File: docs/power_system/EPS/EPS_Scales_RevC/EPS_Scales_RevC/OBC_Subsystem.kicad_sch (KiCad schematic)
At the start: 5 parts, among them U8 INA230

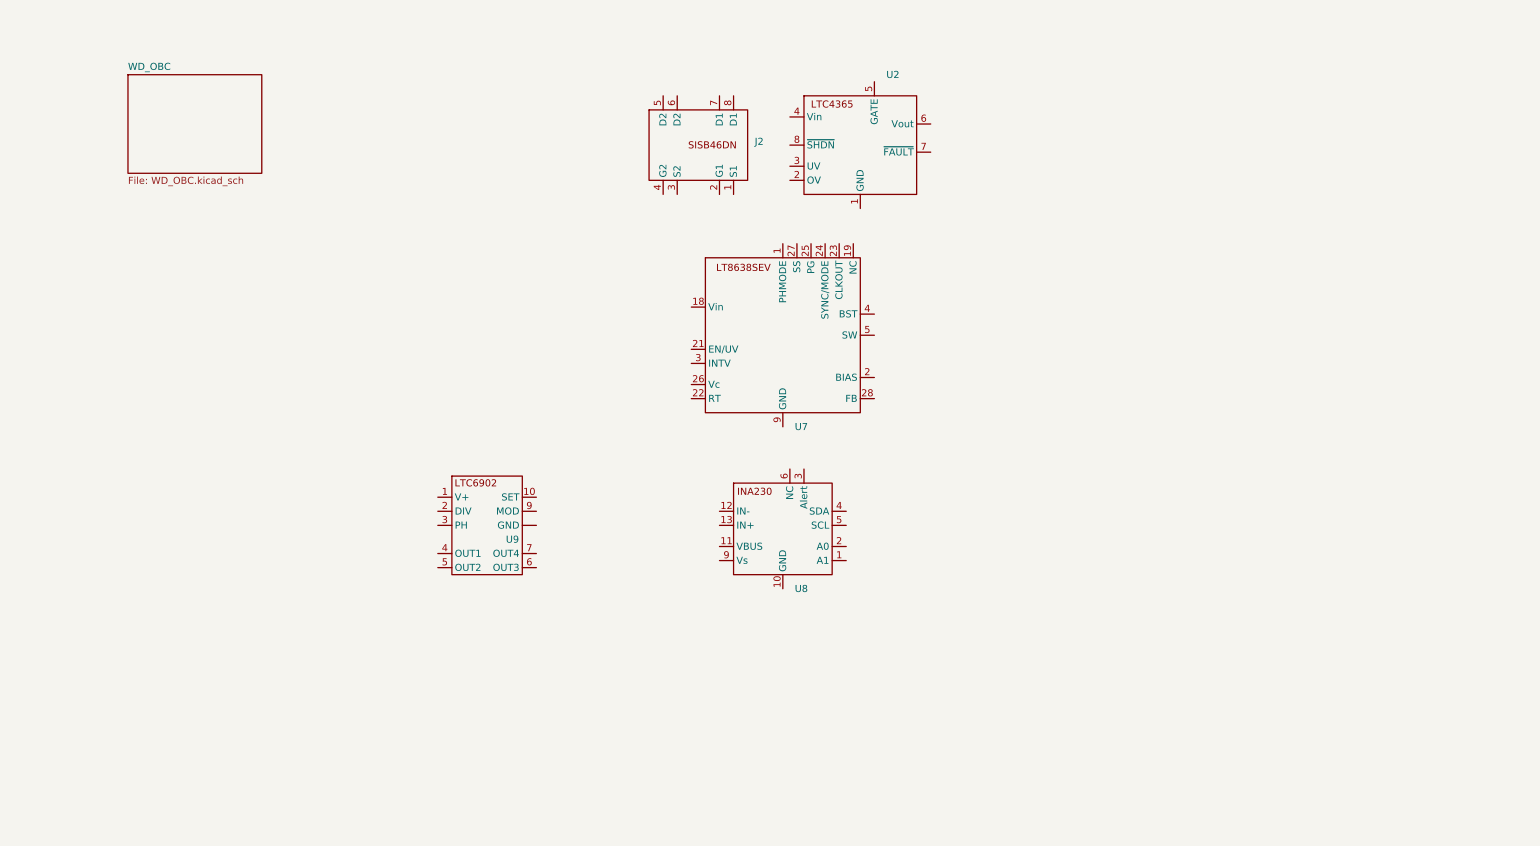
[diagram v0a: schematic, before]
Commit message: Calculations
Lots of behind the scenes stuff going on. Ran through calculations for the Load Switch, Switching Regulator and clock for the jetson using the information from each datasheet. Having to modify these parameters for each subsystem is time consuming as each one requires new calculations. Once this bit is done the schematic will be done, leading to layout. Aiming for thursday Layout.
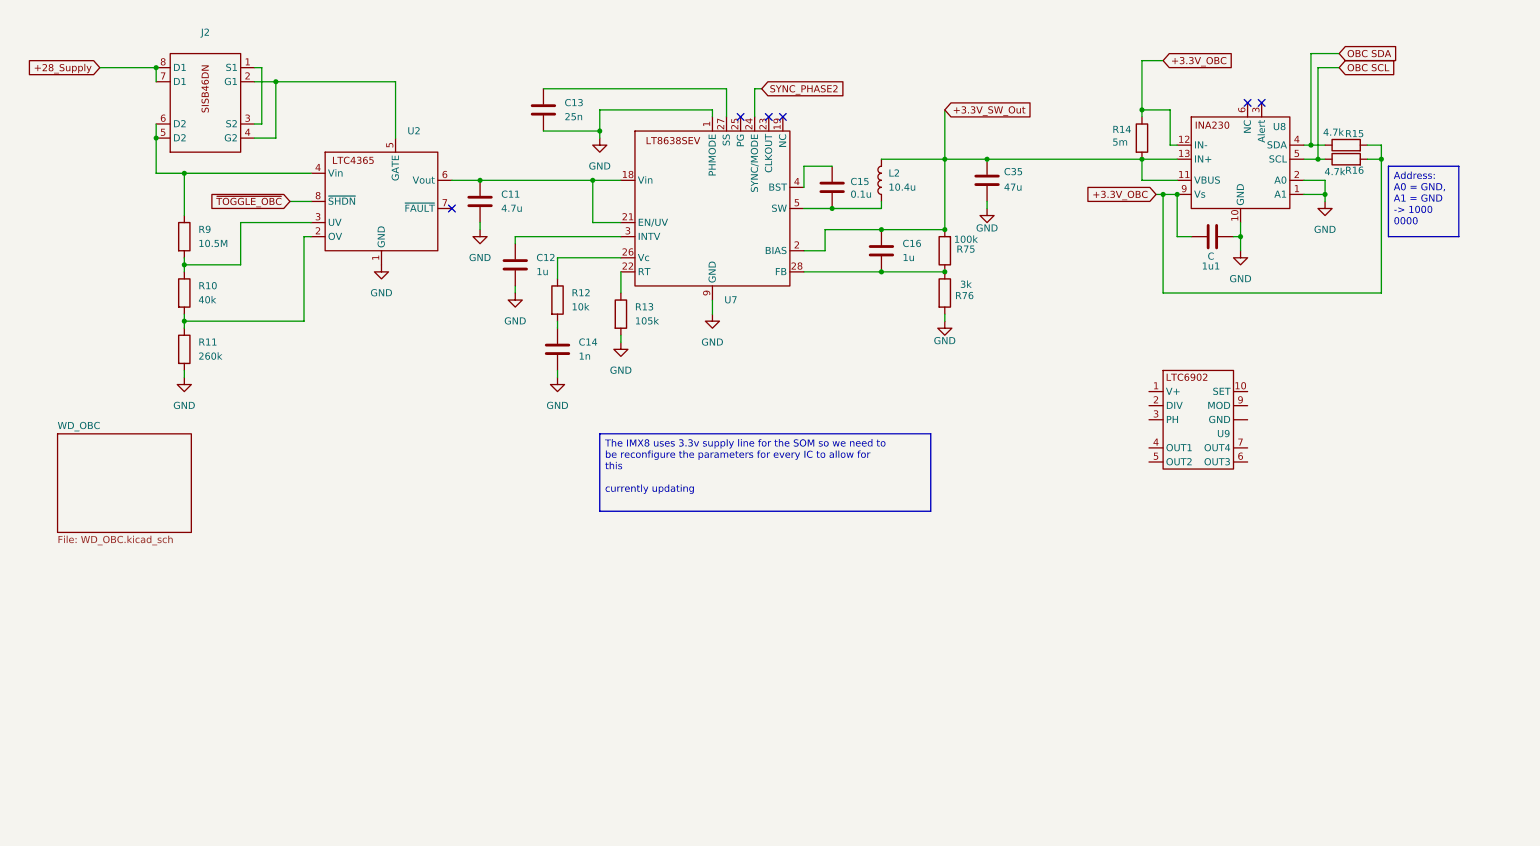
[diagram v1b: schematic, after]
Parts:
- added 1u1: C, symbol Device:C
- added C11: 4.7u, symbol Device:C
- added C12, C16: 1u, symbol Device:C
- added C13: 25n, symbol Device:C
- added C14: 1n, symbol Device:C
- added C15: 0.1u, symbol Device:C
- added C35: 47u, symbol Device:C
- added L2: 10.4u, symbol Device:L
- added R10: 40k, symbol Device:R
- added R11: 260k, symbol Device:R
- added R12: 10k, symbol Device:R
- added R13: 105k, symbol Device:R
- added R14: 5m, symbol Device:R
- added R15, R16: 4.7k, symbol Device:R
- added R75: 100k, symbol Device:R
- added R76: 3k, symbol Device:R
- added R9: 10.5M, symbol Device:R
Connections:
- net GND: now reaches U8.1 (A1)
- net GND: now also U2.1 (GND), U7.1 (PHMODE), U7.9 (GND), U8.10 (GND), U8.2 (A0), 1u1.1, C11.2, C12.2, C13.2, C14.2, C35.2, R11.2, R13.2, R76.2
- net +3.3V_SW_Out: now reaches U8.11 (VBUS)
- net +3.3V_SW_Out: now also U7.2 (BIAS), U8.13 (IN+), C16.1, C35.1, L2.2, R14.2, R75.2
- net +3.3V_OBC: now reaches U8.12 (IN-)
- net +3.3V_OBC: now also U8.9 (Vs), 1u1.2, R14.1, R15.2, R16.2
- net OBC SDA: now reaches U8.4 (SDA)
- net OBC SDA: now also R15.1
- net OBC SCL: now reaches U8.5 (SCL)
- net OBC SCL: now also R16.1
- net at U7.18 (Vin): now also U2.6 (Vout), U7.21 (EN/UV), C11.1
- net at U7.22 (RT): now also R13.1
- net SYNC_PHASE2: now reaches U7.24 (SYNC/MODE)
- net at U7.26 (Vc): now also R12.1
- net at U7.27 (SS): now also C13.1
- net at U7.28 (FB): now also C16.2, R75.1, R76.1
- net at U7.3 (INTV): now also C12.1
- net at U7.4 (BST): now also C15.1
- net at U7.5 (SW): now also C15.2, L2.1
- net at J2.1 (S1): now also J2.3 (S2)
- net at J2.2 (G1): now also J2.4 (G2), U2.5 (GATE)
- net at J2.5 (D2): now also J2.6 (D2), U2.4 (Vin), R9.1
- net +28_Supply: now reaches J2.7 (D1)
- net +28_Supply: now also J2.8 (D1)
- net at U2.2 (OV): now also R10.2, R11.1
- net at U2.3 (UV): now also R10.1, R9.2
- net ~{TOGGLE_OBC}: now reaches U2.8 (~{SHDN})
- new net: C14.1, R12.2
- no-connect marks 0 -> 6
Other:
- moved on the sheet: U9

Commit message: Rev C. Schematic 90 % Complete
All EPS components for each subsystem implemented. Only errors and warning are relating to missing peripheral connections and connectors which will be discussed tomorrow when I go to the lab.
Calculations are done as well.
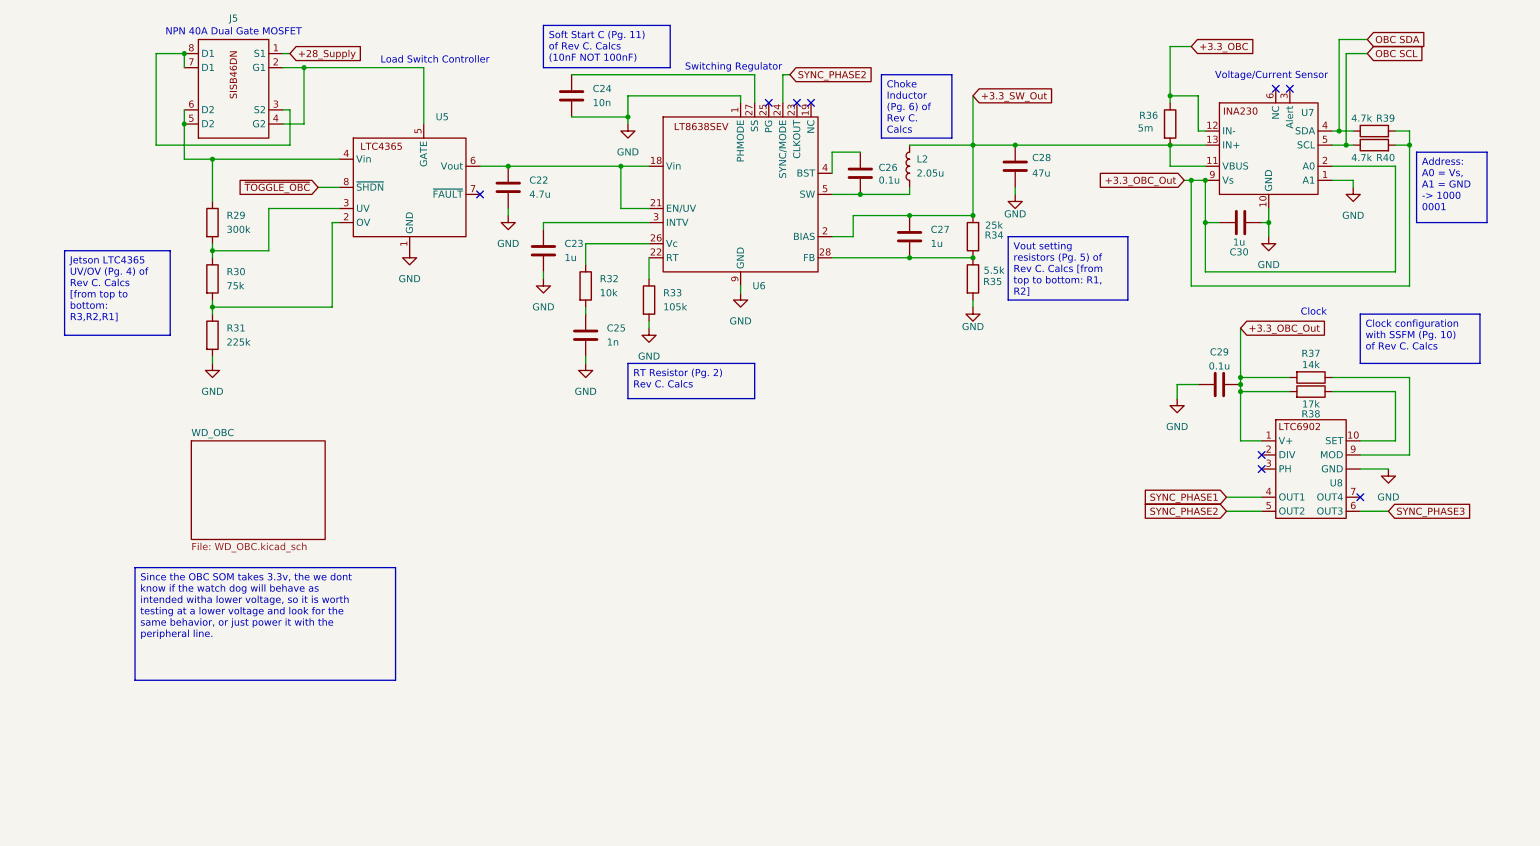
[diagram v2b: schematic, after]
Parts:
- removed 1u1: C, symbol Device:C
- removed C11: 4.7u, symbol Device:C
- removed C12, C16: 1u, symbol Device:C
- removed C13: 25n, symbol Device:C
- removed C14: 1n, symbol Device:C
- removed C15: 0.1u, symbol Device:C
- removed C35: 47u, symbol Device:C
- removed J2: ~, RevC Footprints:MOSFET_DN-T1-GE3_VIS, symbol SISB46DN:SISB46DN
- removed R10: 40k, symbol Device:R
- removed R11: 260k, symbol Device:R
- removed R12: 10k, symbol Device:R
- removed R13: 105k, symbol Device:R
- removed R14: 5m, symbol Device:R
- removed R15, R16: 4.7k, symbol Device:R
- removed R75: 100k, symbol Device:R
- removed R76: 3k, symbol Device:R
- removed R9: 10.5M, symbol Device:R
- removed U2: ~, RevC Footprints:LTC4365, symbol LTC4365:LTC4365
- removed U7: ~, RevC Footprints:LT8638SEVPBF, symbol LT8638SEV#PBF:LT863SEV#PBF
- removed U8: INA230, RevC Footprints:INA230AIRGTT, symbol INA230:INA230 [RGT PACKAGE]
- added C22: 4.7u, symbol Device:C
- added C23, C27, C30: 1u, symbol Device:C
- added C24: 10n, symbol Device:C
- added C25: 1n, symbol Device:C
- added C26, C29: 0.1u, symbol Device:C
- added C28: 47u, symbol Device:C
- added J5: ~, RevC Footprints:MOSFET_DN-T1-GE3_VIS, symbol SISB46DN:SISB46DN
- added R29: 300k, symbol Device:R
- added R30: 75k, symbol Device:R
- added R31: 225k, symbol Device:R
- added R32: 10k, symbol Device:R
- added R33: 105k, symbol Device:R
- added R34: 25k, symbol Device:R
- added R35: 5.5k, symbol Device:R
- added R36: 5m, symbol Device:R
- added R37: 14k, symbol Device:R
- added R38: 17k, symbol Device:R
- added R39, R40: 4.7k, symbol Device:R
- added U5: ~, RevC Footprints:LTC4365, symbol LTC4365:LTC4365
- added U6: ~, RevC Footprints:LT8638SEVPBF, symbol LT8638SEV#PBF:LT863SEV#PBF
- added U7: INA230, RevC Footprints:INA230AIRGTT, symbol INA230:INA230 [RGT PACKAGE]
- L2: value 10.4u -> 2.05u
- renumbered U9 to U8
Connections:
- net +28_Supply: now also J5.1 (S1)
- net GND: now also U8. (GND), C22.2, C23.2, C24.2, C25.2, C28.2, C29.1, C30.1, R31.2, R33.2, R35.2, U5.1 (GND), U6.1 (PHMODE), U6.9 (GND), U7.1 (A1), U7.10 (GND)
- net OBC SCL: now also R40.1, U7.5 (SCL)
- net OBC SDA: now also R39.1, U7.4 (SDA)
- net SYNC_PHASE2: now also U8.5 (OUT2), U6.24 (SYNC/MODE)
- net ~{TOGGLE_OBC}: now also U5.8 (~{SHDN})
- net at L2.1: now also C26.2, U6.5 (SW)
- net +3.3_OBC_Out: now reaches U8.1 (V+)
- net +3.3_OBC_Out: now also C29.2, C30.2, R37.2, R38.2, R39.2, R40.2, U7.2 (A0), U7.9 (Vs)
- net at U8.10 (SET): now also R38.1
- net SYNC_PHASE1: now reaches U8.4 (OUT1)
- net SYNC_PHASE3: now reaches U8.6 (OUT3)
- net at U8.9 (MOD): now also R37.1
- net +3.3V_SW_Out renamed +3.3_SW_Out
- net +3.3_SW_Out: now also C27.1, C28.1, R34.2, R36.2, U6.2 (BIAS), U7.11 (VBUS), U7.13 (IN+)
- new net: C22.1, U5.6 (Vout), U6.18 (Vin), U6.21 (EN/UV)
- new net: J5.2 (G1), J5.4 (G2), U5.5 (GATE)
- new net: J5.3 (S2), J5.7 (D1), J5.8 (D1)
- new net: J5.5 (D2), J5.6 (D2), R29.1, U5.4 (Vin)
- new net: C27.2, R34.1, R35.1, U6.28 (FB)
- new net: R29.2, R30.1, U5.3 (UV)
- new net: R30.2, R31.1, U5.2 (OV)
- new net: C24.1, U6.27 (SS)
- new net: R33.1, U6.22 (RT)
- new net: R32.1, U6.26 (Vc)
- new net: C23.1, U6.3 (INTV)
- new net: C26.1, U6.4 (BST)
- new net: C25.1, R32.2
- new net +3.3_OBC: R36.1, U7.12 (IN-)
- no-connect marks 6 -> 9
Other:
- note added: "Clock"
- note added: "Load Switch Controller"
- note added: "NPN 40A Dual Gate MOSFET"
- note added: "Switching Regulator"
- note added: "Voltage/Current Sensor"
- moved on the sheet: U8

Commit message: Added Dummy Boards & XNOR functionality
Almost done with Dummy boards, just need to link some gecko footprints to the schematic symbol pins and layout can begin
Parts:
- added U14: 4077, symbol 4xxx:4077
- added U16: ~, symbol OBC_Dummy:OBC
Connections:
- net GND: now also U16.2 (GND)
- net OBC SCL: now also U16.4 (SCL)
- net OBC SDA: now also U16.3 (SDA)
- net +28_Supply renamed +28V_Supply
- net +3.3_OBC renamed +3.3V_OBC
- net +3.3V_OBC: now also U16.1 (+3.3V)
- net +3.3_OBC_Out renamed +3.3V_OBC_Out
- net +3.3V_OBC_Out: now also U16.7 (+3.3V_Out)
- net +3.3_SW_Out: no longer names the net of C27.1, C28.1, L2.2, R34.2, R36.2, U6.2 (BIAS), U7.11 (VBUS), U7.13 (IN+)
- net ~{TOGGLE_OBC}: no longer names the net of U5.8 (~{SHDN})
- net ~{TOGGLE_OBC}: now also U14.4
- new net WDT_WDI_OBC: U16.5 (OBC_WD_PET)
- new net ~{OBC_TOGGLE_OBC}: U14.5, U16.6 (GPIO_~{SHDN})
- new net ~{WD_TOGGLE_OBC}: U14.6
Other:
- note added: "OBC Dummy as placeholder for IMX8"
- moved on the sheet: C29, R37, R38, U8

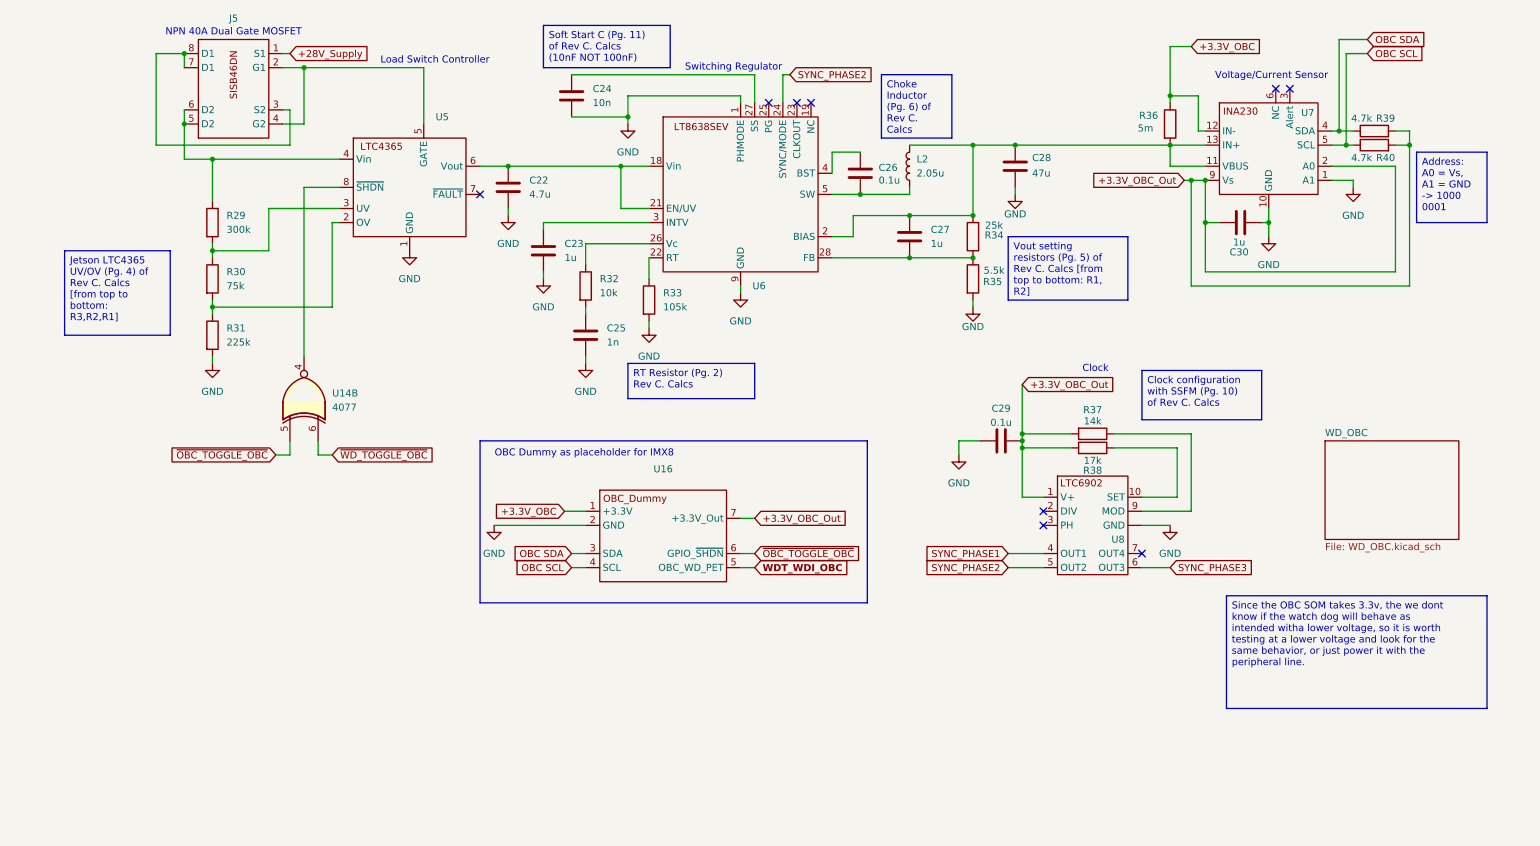
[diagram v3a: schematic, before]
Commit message: Rev C. Layout Started
Footprints and Symbols properly linked. Started organizing PCB layout
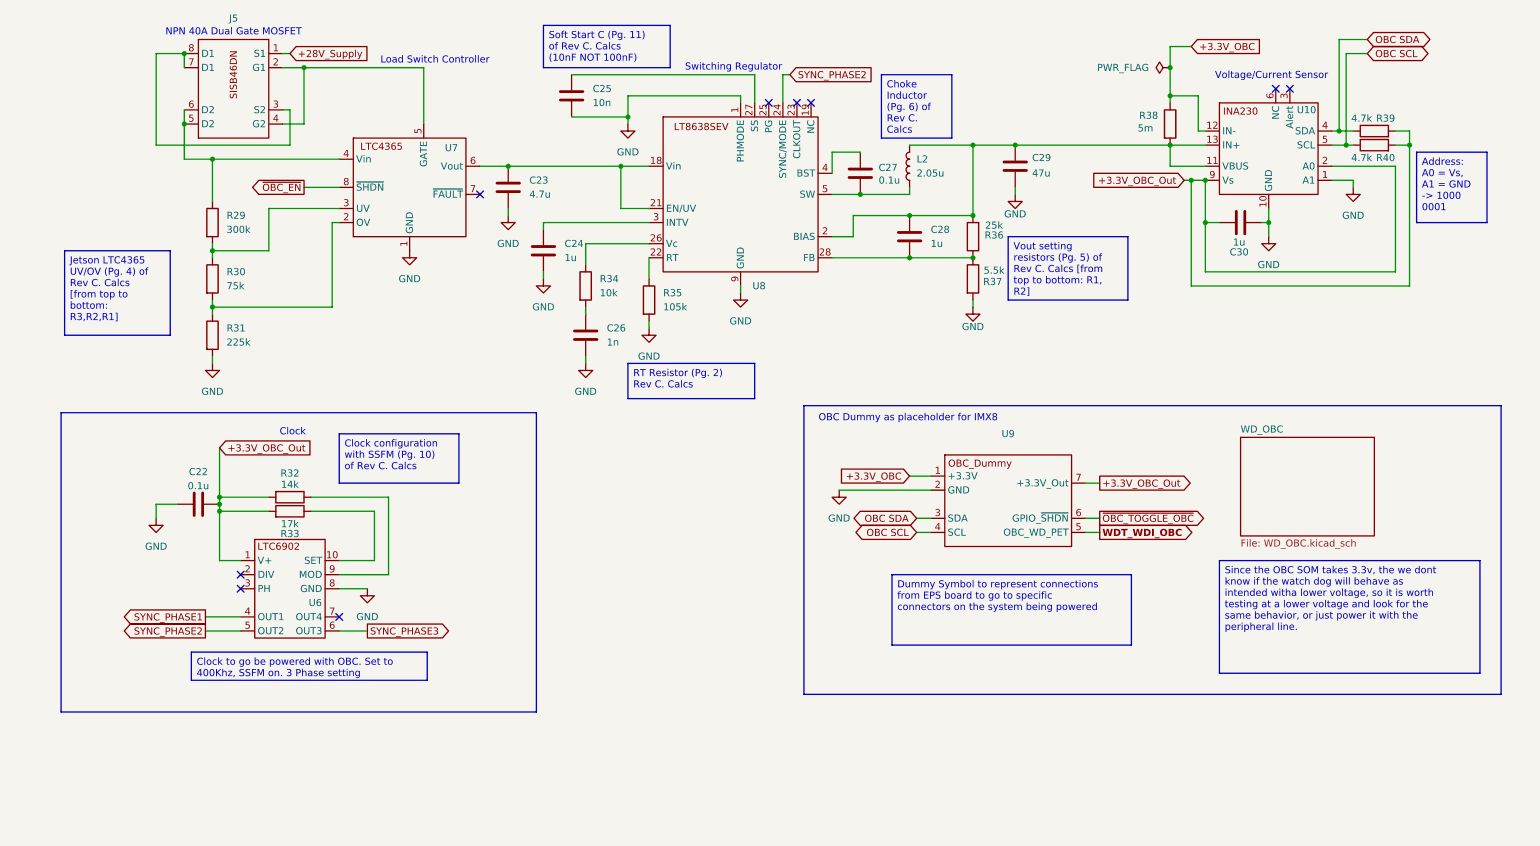
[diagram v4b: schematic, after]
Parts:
- removed U14: 4077, symbol 4xxx:4077
- C22: renamed from C29; footprint (none) -> Capacitor_SMD:C_0603_1608Metric
- C23: renamed from C22; footprint (none) -> Capacitor_SMD:C_0603_1608Metric
- C24: renamed from C23; footprint (none) -> Capacitor_SMD:C_0603_1608Metric
- C25: renamed from C24; footprint (none) -> Capacitor_SMD:C_0603_1608Metric
- C26: renamed from C25; footprint (none) -> Capacitor_SMD:C_0603_1608Metric
- C27: renamed from C26; footprint (none) -> Capacitor_SMD:C_0603_1608Metric
- C28: renamed from C27; footprint (none) -> Capacitor_SMD:C_0603_1608Metric
- C29: renamed from C28; footprint (none) -> Capacitor_SMD:C_0603_1608Metric
- C30: footprint (none) -> Capacitor_SMD:C_0603_1608Metric
- J5: footprint RevC Footprints:MOSFET_DN-T1-GE3_VIS -> RevC Footprints:SISB46DN-T1-GE3
- L2: footprint (none) -> Inductor_SMD:L_0603_1608Metric
- R29, R30, R31, R39, R40: footprint (none) -> Resistor_SMD:R_0603_1608Metric
- R32: renamed from R37; footprint (none) -> Resistor_SMD:R_0603_1608Metric
- R33: renamed from R38; footprint (none) -> Resistor_SMD:R_0603_1608Metric
- R34: renamed from R32; footprint (none) -> Resistor_SMD:R_0603_1608Metric
- R35: renamed from R33; footprint (none) -> Resistor_SMD:R_0603_1608Metric
- R36: renamed from R34; footprint (none) -> Resistor_SMD:R_0603_1608Metric
- R37: renamed from R35; footprint (none) -> Resistor_SMD:R_0603_1608Metric
- R38: renamed from R36; footprint (none) -> Resistor_SMD:R_0603_1608Metric
- U9: renamed from U16; footprint (none) -> Connector_PinSocket_2.54mm:PinSocket_1x07_P2.54mm_Vertical
- renumbered U7 to U10, U8 to U6, U5 to U7, U6 to U8
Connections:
- net GND: now also U6.8 (GND); no longer U6. (GND)
- net ~{OBC_EN}: now reaches U7.8 (~{SHDN})
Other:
- moved on the sheet: C22, R32, R33, U9
